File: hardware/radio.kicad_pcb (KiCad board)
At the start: 2 copper layers, 7.3 x 9.3 mm, 61 parts, among them J1 105450-0101, J2 Conn_01x02, J3 Conn_01x02, J4 Conn_01x04, J5 Conn_01x02_Male, Q1 Q_PMOS_DGS, Q2 Q_NMOS_DGS, Q3 Q_NMOS_DGS, Q4 Q_PMOS_DGS, SW1 SW_BOOT, SW2 SW_RST, SW3 SW_1, SW4 Rot_Enc, SW5 SW_2, SW6 SW_3, U1 TP4056, U2 ESP32-WROOM-32, U3 TPS5432, U4 MAX98357

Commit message: board finished (?)
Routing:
- net +3V3: track 212.7 -> 255.6 mm, vias 2 -> 3
- net GND: track 41.2 -> 54.1 mm, vias 49 -> 100
- added copper zone on B.Cu, net GND
- added copper zone on F.Cu, net GND
- removed copper zone on B.Cu, net (none)
- removed copper zone on F.Cu, net (none)
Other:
- board size 7.3 x 9.3 mm -> 100 x 50 mm

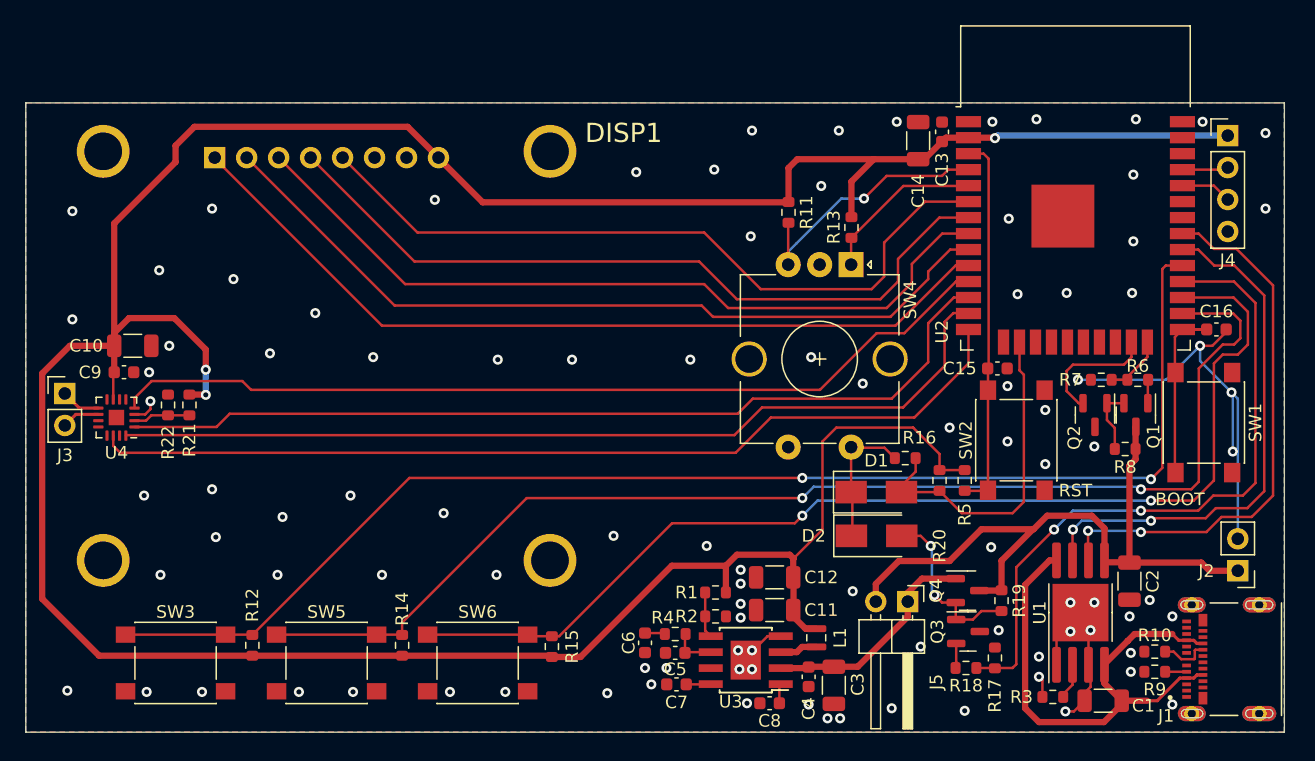
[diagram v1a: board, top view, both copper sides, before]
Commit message: fixed DRC  violations, added silkscreen legend
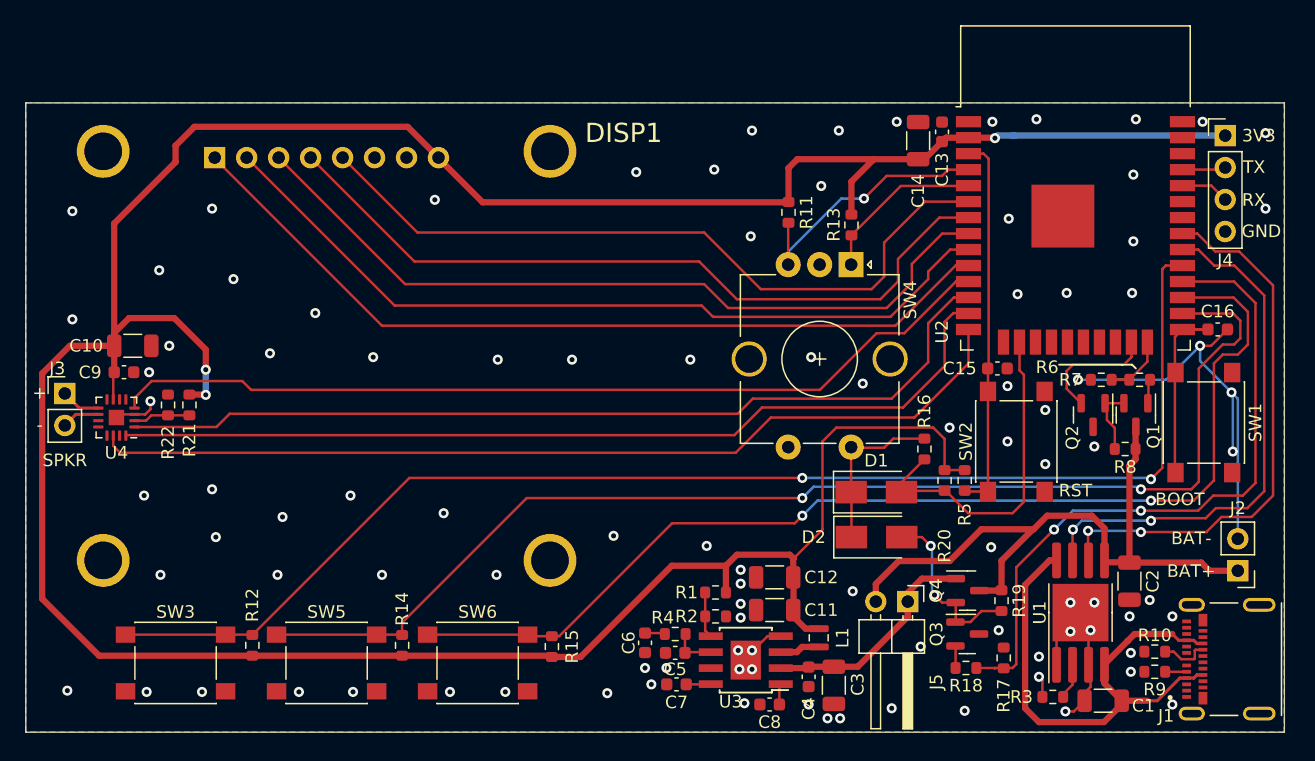
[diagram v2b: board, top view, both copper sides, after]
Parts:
- moved R16 1.69 mm to (101.4, 57.5), turned to 90 degrees
- moved R17 0.70 mm to (107.7, 74.1)
- moved R20 0.40 mm to (103.0, 60.0)
- moved Q3 0.21 mm to (104.8, 72.2)
- moved J4 0.20 mm to (125.3, 32.6)
- moved R13 0.20 mm to (95.6, 39.7)
- moved L1 0.19 mm to (93.0, 72.5)
- moved Q2 0.15 mm to (114.8, 54.8)
- moved R6 0.15 mm to (118.5, 52.0)
- moved C16 0.10 mm to (124.7, 48.0)
- moved SW2 0.10 mm to (108.7, 56.9)
- moved C8 0.10 mm to (89.1, 77.8)
- moved D2 0.10 mm to (97.6, 64.5)
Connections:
- U4 pad 17: (no net) -> GND
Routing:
- net ENC_S1: track 10.9 -> 13.1 mm
- net GND: track 54.1 -> 55.6 mm
- net +3V3: track 255.6 -> 256.3 mm
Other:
- board text added: "+"
- board text added: "-"
- board text added: "3V3"
- board text added: "BAT+"
- board text added: "BAT-"
- board text added: "GND"
- board text added: "RX"
- board text added: "SPKR"
- board text added: "TX"
